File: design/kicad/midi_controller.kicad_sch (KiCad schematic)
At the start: 5 parts, among them J7 Conn_01x05, U1 CD74HC4067M

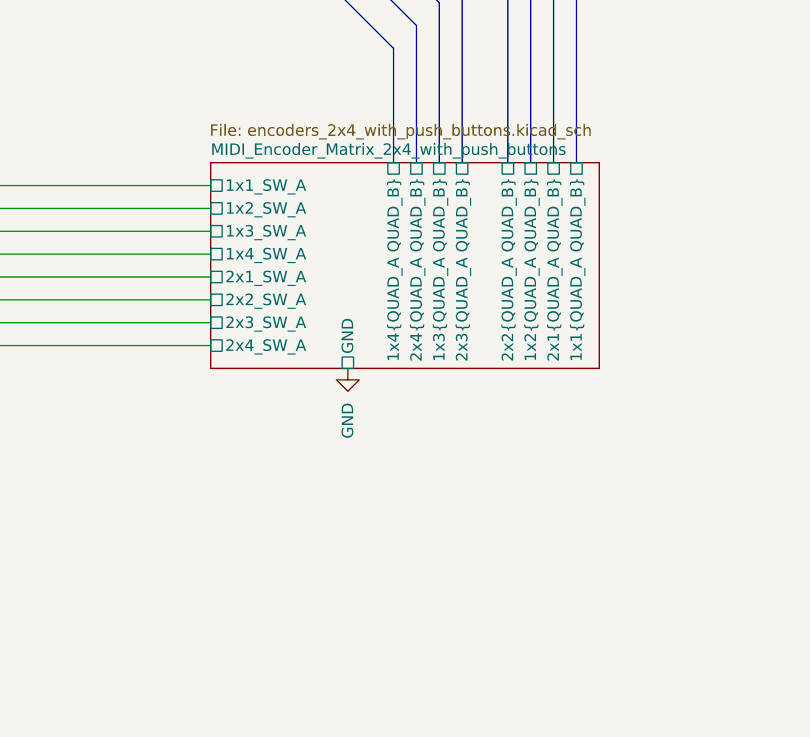
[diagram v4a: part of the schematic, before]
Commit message: Refactor MIDI controller design files
- Cleaned up hidden nets and net classes in the PCB layout file to improve clarity and maintainability.
- Adjusted visible layers to enhance the design view.
- Updated column widths in the properties section for better alignment.
- Modified schematic file by removing unnecessary wire elements and adding new ones for improved layout.
- Adjusted positions of various components and pins to ensure proper alignment and functionality.
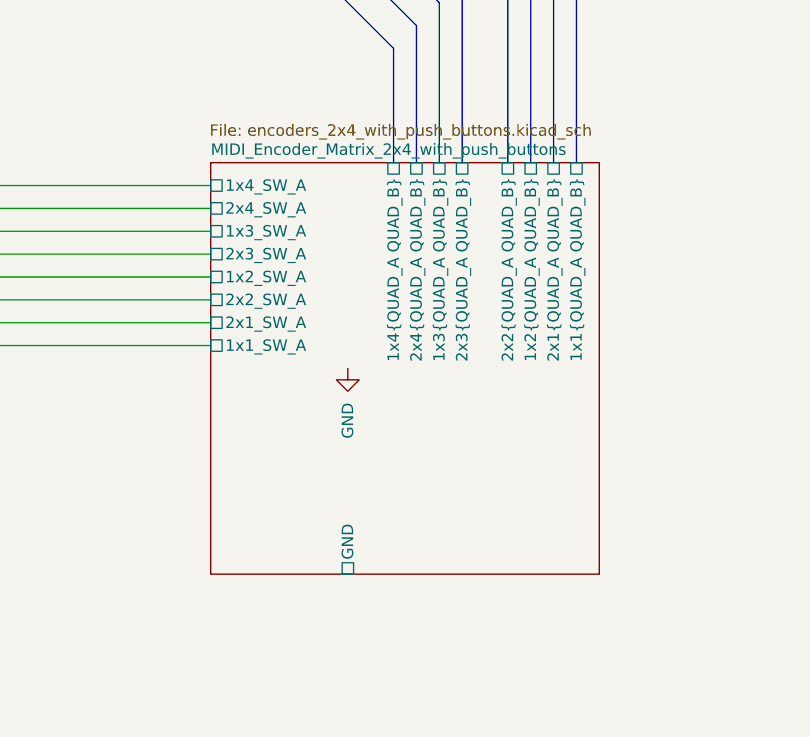
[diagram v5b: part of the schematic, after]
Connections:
- net MIDI_Encoder_Matrix_2x4_with_push_buttons/1x1_SW_A: now also U1.2 (I7); no longer U1.9 (I0)
- net MIDI_Encoder_Matrix_2x4_with_push_buttons/1x2_SW_A: now also U1.5 (I4); no longer U1.8 (I1)
- net MIDI_Encoder_Matrix_2x4_with_push_buttons/1x4_SW_A: now also U1.9 (I0); no longer U1.6 (I3)
- net MIDI_Encoder_Matrix_2x4_with_push_buttons/2x1_SW_A: now also U1.3 (I6); no longer U1.5 (I4)
- net MIDI_Encoder_Matrix_2x4_with_push_buttons/2x3_SW_A: now also U1.6 (I3); no longer U1.3 (I6)
- net MIDI_Encoder_Matrix_2x4_with_push_buttons/2x4_SW_A: now also U1.8 (I1); no longer U1.2 (I7)
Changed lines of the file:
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@@
 	(wire
 		(pts
-			(xy 72.39 171.45) (xy 278.13 171.45)
-		)
-		(stroke
-			(width 0)
-			(type default)
-		)
-	)
-	(wire
-		(pts
 			(xy 101.6 231.14) (xy 101.6 191.77)
 		)
@@
 	(wire
 		(pts
-			(xy 254 101.6) (xy 251.46 104.14)
+			(xy 72.39 166.37) (xy 278.13 166.37)
 		)
 		(stroke
@@
 	(wire
 		(pts
-			(xy 240.03 99.06) (xy 251.46 99.06)
+			(xy 254 101.6) (xy 251.46 104.14)
 		)
 		(stroke
@@
 		)
 	)
-	(bus
+	(wire
 		(pts
-			(xy 274.32 119.38) (xy 298.45 143.51)
+			(xy 240.03 99.06) (xy 251.46 99.06)
 		)
 		(stroke
@@
 		)
 	)
-	(wire
+	(bus
 		(pts
-			(xy 240.03 88.9) (xy 251.46 88.9)
+			(xy 274.32 119.38) (xy 298.45 143.51)
 		)
 		(stroke
@@
 	(wire
 		(pts
-			(xy 72.39 163.83) (xy 278.13 163.83)
+			(xy 240.03 88.9) (xy 251.46 88.9)
 		)
 		(stroke
@@
 	(wire
 		(pts
+			(xy 72.39 176.53) (xy 278.13 176.53)
+		)
+		(stroke
+			(width 0)
+			(type default)
+		)
+	)
+	(wire
+		(pts
 			(xy 168.91 92.71) (xy 168.91 76.2)
 		)
@@
 		)
 	)
+	(wire
+		(pts
+			(xy 72.39 168.91) (xy 278.13 168.91)
+		)
+		(stroke
+			(width 0)
+			(type default)
+		)
+	)
 	(bus
 		(pts
@@
 	(wire
 		(pts
+			(xy 72.39 158.75) (xy 278.13 158.75)
+		)
+		(stroke
+			(width 0)
+			(type default)
+		)
+	)
+	(wire
+		(pts
 			(xy 240.03 86.36) (xy 251.46 86.36)
 		)
@@
 	(wire
 		(pts
-			(xy 72.39 166.37) (xy 278.13 166.37)
+			(xy 240.03 91.44) (xy 251.46 91.44)
 		)
 		(stroke
@@
 	(wire
 		(pts
-			(xy 240.03 91.44) (xy 251.46 91.44)
+			(xy 72.39 163.83) (xy 278.13 163.83)
 		)
 		(stroke
@@
 	(wire
 		(pts
-			(xy 72.39 161.29) (xy 278.13 161.29)
-		)
-		(stroke
-			(width 0)
-			(type default)
-		)
-	)
-	(wire
-		(pts
 			(xy 44.45 191.77) (xy 44.45 209.55)
 		)
@@
 	(wire
 		(pts
-			(xy 72.39 168.91) (xy 278.13 168.91)
-		)
-		(stroke
-			(width 0)
-			(type default)
-		)
-	)
-	(wire
-		(pts
 			(xy 106.68 186.69) (xy 72.39 186.69)
 		)
@@
 	(wire
 		(pts
-			(xy 72.39 176.53) (xy 278.13 176.53)
+			(xy 240.03 96.52) (xy 251.46 96.52)
 		)
 		(stroke
@@
 	(wire
 		(pts
-			(xy 240.03 96.52) (xy 251.46 96.52)
+			(xy 133.35 102.87) (xy 171.45 102.87)
 		)
 		(stroke
@@
 	(wire
 		(pts
-			(xy 133.35 102.87) (xy 171.45 102.87)
+			(xy 147.32 121.92) (xy 184.15 121.92)
 		)
 		(stroke
@@
 	(wire
 		(pts
-			(xy 147.32 121.92) (xy 184.15 121.92)
+			(xy 104.14 189.23) (xy 104.14 228.6)
 		)
 		(stroke
@@
 	(wire
 		(pts
-			(xy 104.14 189.23) (xy 104.14 228.6)
+			(xy 72.39 173.99) (xy 278.13 173.99)
 		)
 		(stroke
@@
 	(wire
 		(pts
+			(xy 72.39 161.29) (xy 278.13 161.29)
+		)
+		(stroke
+			(width 0)
+			(type default)
+		)
+	)
+	(wire
+		(pts
 			(xy 240.03 104.14) (xy 251.46 104.14)
 		)
@@
 	(wire
 		(pts
-			(xy 336.55 116.84) (xy 344.17 116.84)
+			(xy 72.39 171.45) (xy 278.13 171.45)
 		)
 		(stroke
@@
 		)
 	)
-	(bus
+	(wire
 		(pts
-			(xy 269.24 88.9) (xy 313.69 133.35)
+			(xy 336.55 116.84) (xy 344.17 116.84)
 		)
 		(stroke
@@
 	(bus
 		(pts
-			(xy 306.07 137.16) (xy 267.97 99.06)
+			(xy 269.24 88.9) (xy 313.69 133.35)
 		)
 		(stroke
@@
 		)
 	)
-	(wire
+	(bus
 		(pts
-			(xy 115.57 233.68) (xy 99.06 233.68)
+			(xy 306.07 137.16) (xy 267.97 99.06)
 		)
 		(stroke
@@
 	(wire
 		(pts
-			(xy 336.55 107.95) (xy 337.82 109.22)
+			(xy 115.57 233.68) (xy 99.06 233.68)
 		)
 		(stroke
@@
 	(wire
 		(pts
-			(xy 72.39 158.75) (xy 278.13 158.75)
+			(xy 336.55 107.95) (xy 337.82 109.22)
 		)
 		(stroke
@@
 	(wire
 		(pts
-			(xy 72.39 173.99) (xy 278.13 173.99)
-		)
-		(stroke
-			(width 0)
-			(type default)
-		)
-	)
-	(wire
-		(pts
 			(xy 46.99 191.77) (xy 44.45 191.77)
 		)
@@
 	(sheet
 		(at 278.13 156.21)
-		(size 43.18 22.86)
+		(size 43.18 45.72)
 		(exclude_from_sim no)
 		(in_bom yes)
@@
 		)
 		(pin "GND" passive
-			(at 293.37 179.07 270)
+			(at 293.37 201.93 270)
 			(effects
 				(font
@@
 		)
 		(pin "2x4_SW_A" passive
-			(at 278.13 176.53 180)
+			(at 278.13 161.29 180)
 			(effects
 				(font
@@
 		)
 		(pin "2x1_SW_A" passive
-			(at 278.13 168.91 180)
+			(at 278.13 173.99 180)
 			(effects
 				(font
@@
 		)
 		(pin "1x2_SW_A" passive
-			(at 278.13 161.29 180)
+			(at 278.13 168.91 180)
 			(effects
 				(font
@@
 		)
 		(pin "1x4_SW_A" passive
-			(at 278.13 166.37 180)
+			(at 278.13 158.75 180)
 			(effects
 				(font
@@
 		)
 		(pin "1x1_SW_A" passive
-			(at 278.13 158.75 180)
+			(at 278.13 176.53 180)
 			(effects
 				(font
@@
 		)
 		(pin "2x3_SW_A" passive
-			(at 278.13 173.99 180)
+			(at 278.13 166.37 180)
 			(effects
 				(font

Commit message: Refactor code structure for improved readability and maintainability
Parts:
- added C1, C2, C3, C4: 100n, Capacitor_SMD:C_0805_2012Metric, symbol Device:C
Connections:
- net +3V3: now also C2.1, C4.1
- net +5V: now also C1.2, C3.1
- net GND: now also MCU1.34 (GND), C1.1, C2.2, C3.2, C4.2
- no-connect marks 0 -> 17

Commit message: Refactor code structure for improved readability and maintainability
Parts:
- added D2: SS34, Diode_SMD:D_SMA, symbol Diode:SS34
- added D3: SMAJ5.0CA, Diode_SMD:D_SMA, symbol Diode:SMAJ5.0CA
- added D37, D38, D39, D40: PESD5V0L1BA,115, KiCad:SOD2512X110N, symbol PESD5V0L1BA_115:PESD5V0L1BA,115
- added F1: Fuse, Fuse:Fuse_0805_2012Metric, symbol Device:Fuse
- renumbered C2 to C1, C1 to C2, J7 to J1
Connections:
- net +5V: now also D2.2 (A), D3.1 (A1); no longer MCU1.48 (VIN)
- net GND: now also D3.2 (A2), D37.2 (K2), D38.2 (K2), D39.2 (K2), D40.2 (K2)
- net S0: now also D37.1 (K1)
- net S1: now also D38.1 (K1)
- net S2: now also D39.1 (K1)
- net S3: now also D40.1 (K1)
- new net: F1.1, MCU1.48 (VIN)
- new net: D2.1 (K), F1.2
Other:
- moved on the sheet: C1, C2, C3, C4, D1, ENC_OPT1, J1, MCU1, U1

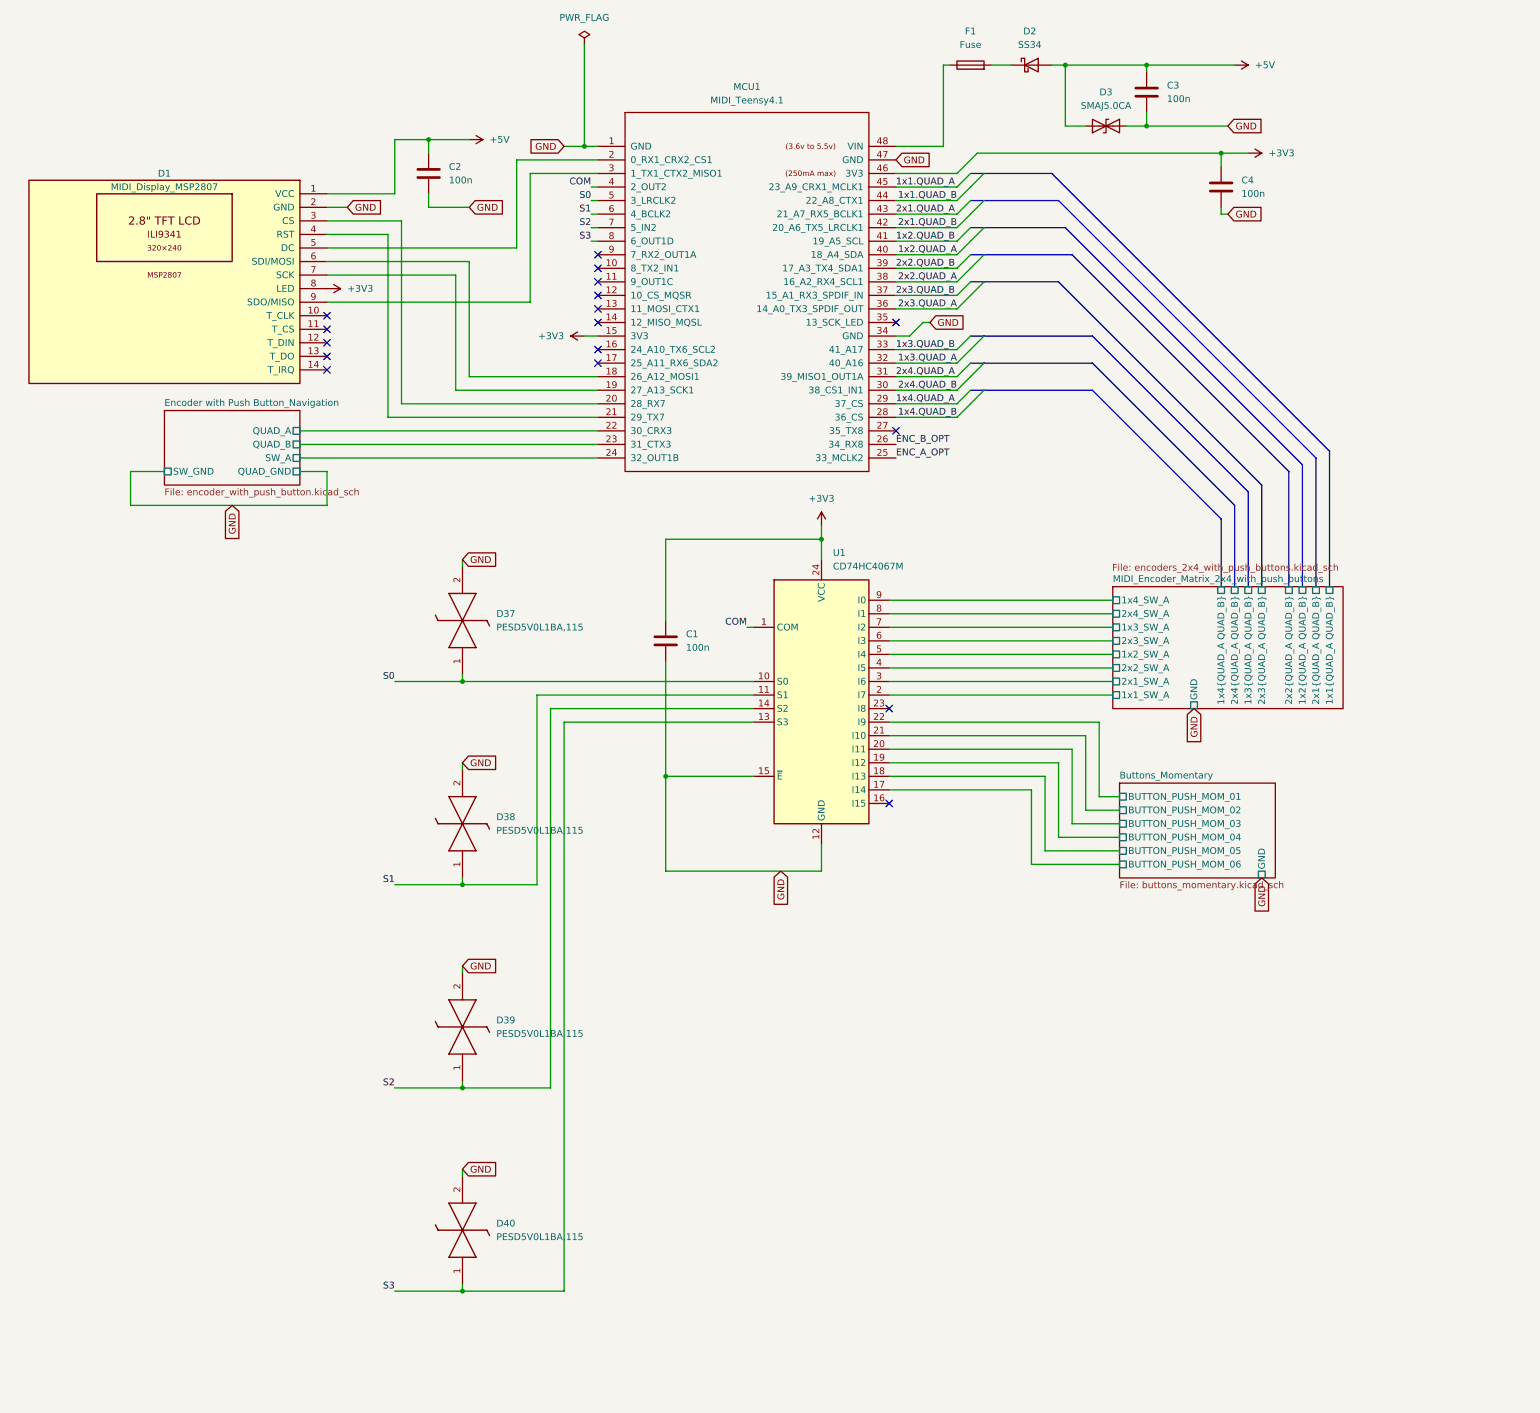
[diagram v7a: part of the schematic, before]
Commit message: Add schematic for MIDI Display MSP2807 with associated components
- Created a new schematic file for the MIDI Display MSP2807.
- Included a unpolarized capacitor (C2) with a value of 100nF.
- Added properties such as reference, value, footprint, and datasheet for the capacitor.
- Integrated the MIDI Display module with detailed pin configurations and properties.
- Defined hierarchical labels for power and data connections (VCC, GND, CS, RST, DC, etc.).
- Ensured all components are marked for BOM inclusion and simulation.
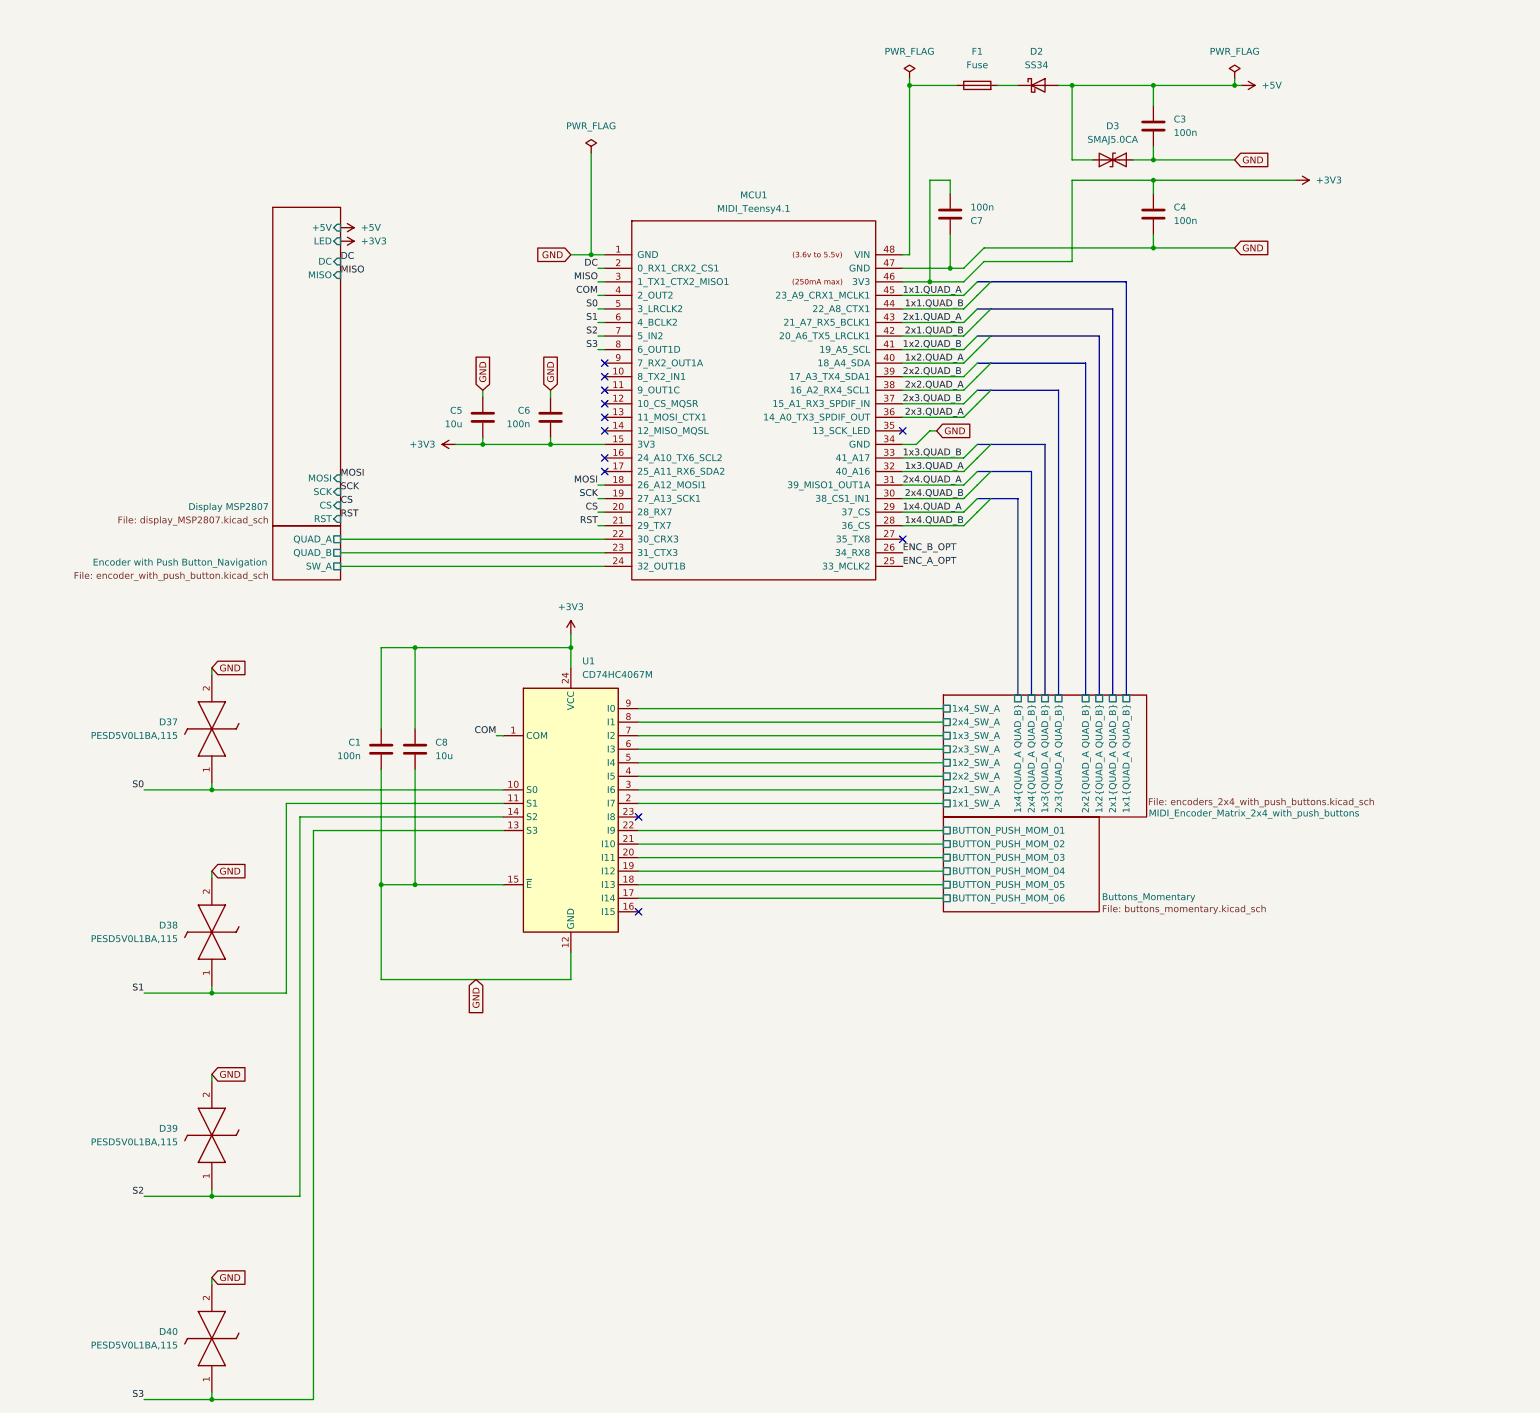
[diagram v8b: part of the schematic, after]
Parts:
- removed C2: 100n, Capacitor_SMD:C_0805_2012Metric, symbol Device:C
- removed D1: MIDI_Display_MSP2807, midi_controller:MSP2807_ILI9341_Display, symbol midi_controller:MIDI_Display_MSP2807
- added C5, C8: 10u, Capacitor_SMD:C_0805_2012Metric, symbol Device:C
- added C6, C7: 100n, Capacitor_SMD:C_0603_1608Metric, symbol Device:C
- C1: footprint Capacitor_SMD:C_0805_2012Metric -> Capacitor_SMD:C_0603_1608Metric
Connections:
- net +3V3: now also C5.1, C6.1, C7.1, C8.1
- net GND: now also C5.2, C6.2, C7.2, C8.2
- net CS: now reaches MCU1.20 (28_RX7)
- net RST: now reaches MCU1.21 (29_TX7)
- net DC: now reaches MCU1.2 (0_RX1_CRX2_CS1)
- net MOSI: now reaches MCU1.18 (26_A12_MOSI1)
- net SCK: now reaches MCU1.19 (27_A13_SCK1)
- net MISO: now reaches MCU1.3 (1_TX1_CTX2_MISO1)
- no-connect marks 17 -> 12
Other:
- added sheet Display MSP2807 (display_MSP2807.kicad_sch)
- sheet Buttons_Momentary ports: added none; removed GND
- sheet Encoder with Push Button_Navigation ports: added none; removed QUAD_GND, SW_GND
- sheet MIDI_Encoder_Matrix_2x4_with_push_buttons ports: added none; removed GND
- moved on the sheet: C1, C3, C4, D2, D3, D37, D38, D39, D40, F1, MCU1, U1
